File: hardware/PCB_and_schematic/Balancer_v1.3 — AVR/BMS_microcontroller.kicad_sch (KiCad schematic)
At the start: 73 parts, among them J12 V_MEAS, J13 LED, J14 ICP, J15 RS485, J16 RS485, Q21 BC817, U10 B0505S-1W, U11 ST485, U12 INA226, U4 AVR64DD28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

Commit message: add bms pcb balacer and smps separated
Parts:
- removed H2, H6, H8: MountingHole, My-Footprints:Mount-Hole-3mm, symbol Mechanical:MountingHole
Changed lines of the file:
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@@
 	)
 	(symbol
-		(lib_id "Mechanical:MountingHole")
-		(at 302.26 199.39 0)
-		(unit 1)
-		(exclude_from_sim yes)
-		(in_bom no)
-		(on_board yes)
-		(dnp no)
-		(fields_autoplaced yes)
-		(property "Reference" "H6"
-			(at 304.8 198.1199 0)
-			(effects
-				(font
-					(size 1.27 1.27)
-				)
-				(justify left)
-			)
-		)
-		(property "Value" "MountingHole"
-			(at 304.8 200.6599 0)
-			(effects
-				(font
-					(size 1.27 1.27)
-				)
-				(justify left)
-			)
-		)
-		(property "Footprint" "My-Footprints:Mount-Hole-3mm"
-			(at 302.26 199.39 0)
-			(effects
-				(font
-					(size 1.27 1.27)
-				)
-				(hide yes)
-			)
-		)
-		(property "Datasheet" "~"
-			(at 302.26 199.39 0)
-			(effects
-				(font
-					(size 1.27 1.27)
-				)
-				(hide yes)
-			)
-		)
-		(property "Description" "Mounting Hole without connection"
-			(at 302.26 199.39 0)
-			(effects
-				(font
-					(size 1.27 1.27)
-				)
-				(hide yes)
-			)
-		)
-		(instances
-			(project "Balancer"
-				(path "/555ba40f-9abb-4b99-82c6-07e888fda9fd/3b90ff07-e5cb-404b-939d-de320e975ba1"
-					(reference "H6")
-					(unit 1)
-				)
-			)
-		)
-	)
-	(symbol
 		(lib_id "power:GND")
 		(at 213.36 118.11 0)
@@
 	)
 	(symbol
-		(lib_id "Mechanical:MountingHole")
-		(at 280.67 214.63 0)
-		(unit 1)
-		(exclude_from_sim yes)
-		(in_bom no)
-		(on_board yes)
-		(dnp no)
-		(fields_autoplaced yes)
-		(property "Reference" "H2"
-			(at 283.21 213.3599 0)
-			(effects
-				(font
-					(size 1.27 1.27)
-				)
-				(justify left)
-			)
-		)
-		(property "Value" "MountingHole"
-			(at 283.21 215.8999 0)
-			(effects
-				(font
-					(size 1.27 1.27)
-				)
-				(justify left)
-			)
-		)
-		(property "Footprint" "My-Footprints:Mount-Hole-3mm"
-			(at 280.67 214.63 0)
-			(effects
-				(font
-					(size 1.27 1.27)
-				)
-				(hide yes)
-			)
-		)
-		(property "Datasheet" "~"
-			(at 280.67 214.63 0)
-			(effects
-				(font
-					(size 1.27 1.27)
-				)
-				(hide yes)
-			)
-		)
-		(property "Description" "Mounting Hole without connection"
-			(at 280.67 214.63 0)
-			(effects
-				(font
-					(size 1.27 1.27)
-				)
-				(hide yes)
-			)
-		)
-		(instances
-			(project "Balancer"
-				(path "/555ba40f-9abb-4b99-82c6-07e888fda9fd/3b90ff07-e5cb-404b-939d-de320e975ba1"
-					(reference "H2")
-					(unit 1)
-				)
-			)
-		)
-	)
-	(symbol
 		(lib_id "power:GND")
 		(at 273.05 106.68 0)
@@
 					(unit 1)
 				)
-			)
-		)
-	)
-	(symbol
-		(lib_id "Mechanical:MountingHole")
-		(at 302.26 209.55 0)
-		(unit 1)
-		(exclude_from_sim yes)
-		(in_bom no)
-		(on_board yes)
-		(dnp no)
-		(fields_autoplaced yes)
-		(property "Reference" "H8"
-			(at 304.8 208.2799 0)
-			(effects
-				(font
-					(size 1.27 1.27)
-				)
-				(justify left)
-			)
-		)
-		(property "Value" "MountingHole"
-			(at 304.8 210.8199 0)
-			(effects
-				(font
-					(size 1.27 1.27)
-				)
-				(justify left)
-			)
-		)
-		(property "Footprint" "My-Footprints:Mount-Hole-3mm"
-			(at 302.26 209.55 0)
-			(effects
-				(font
-					(size 1.27 1.27)
-				)
-				(hide yes)
-			)
-		)
-		(property "Datasheet" "~"
-			(at 302.26 209.55 0)
-			(effects
-				(font
-					(size 1.27 1.27)
-				)
-				(hide yes)
-			)
-		)
-		(property "Description" "Mounting Hole without connection"
-			(at 302.26 209.55 0)
-			(effects
-				(font
-					(size 1.27 1.27)
-				)
-				(hide yes)
-			)
-		)
-		(instances
-			(project "Balancer"
-				(path "/555ba40f-9abb-4b99-82c6-07e888fda9fd/3b90ff07-e5cb-404b-939d-de320e975ba1"
-					(reference "H8")
-					(unit 1)
-				)

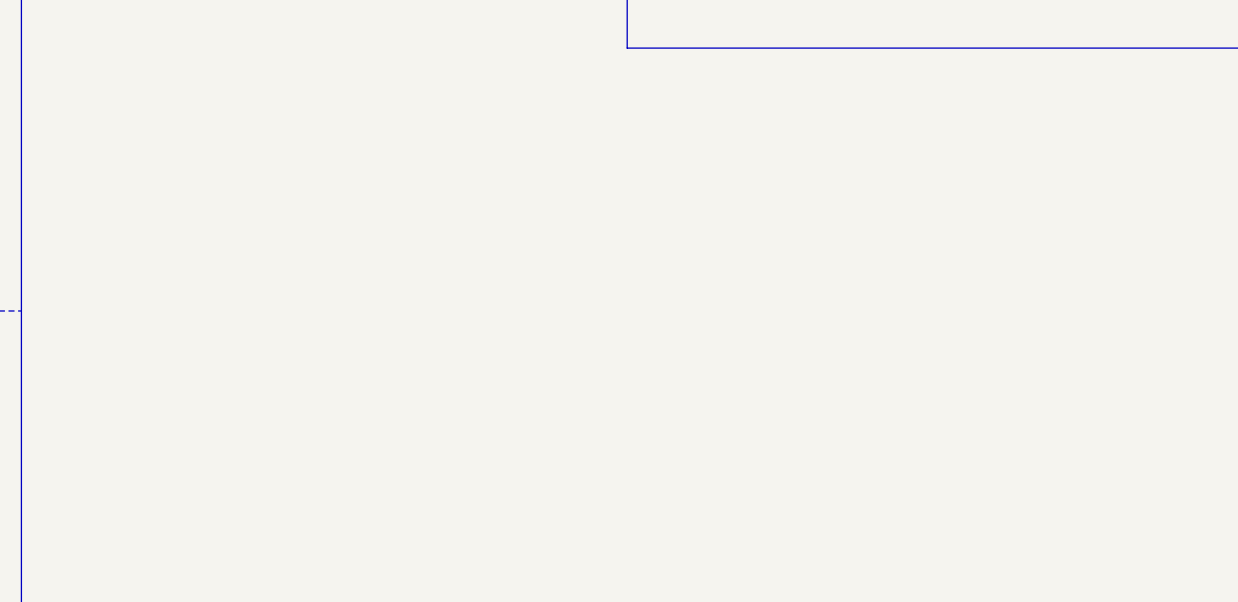
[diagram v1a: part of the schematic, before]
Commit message: routing power module
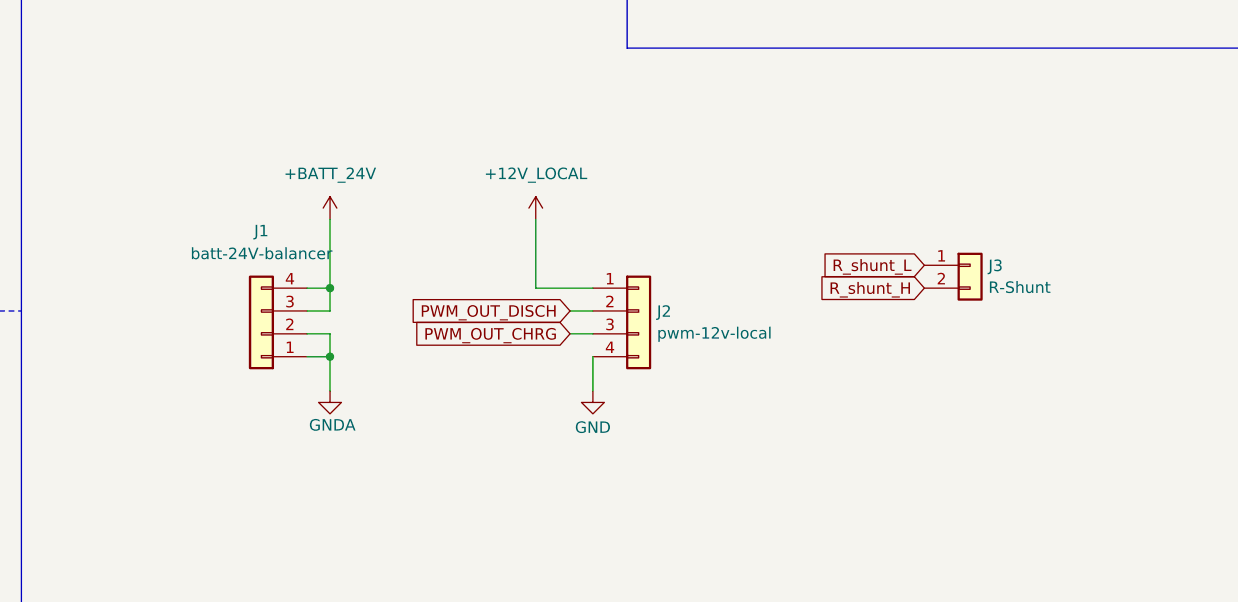
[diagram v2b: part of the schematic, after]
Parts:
- added J1: batt-24V-balancer, Connector_PinSocket_2.54mm:PinSocket_1x04_P2.54mm_Vertical, symbol Connector_Generic:Conn_01x04
- added J2: pwm-12v-local, Connector_PinSocket_2.54mm:PinSocket_1x04_P2.54mm_Vertical, symbol Connector_Generic:Conn_01x04
- added J3: R-Shunt, Connector_PinHeader_2.54mm:PinHeader_1x02_P2.54mm_Vertical, symbol Connector_Generic:Conn_01x02
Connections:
- net +12V_LOCAL: now also J2.1 (Pin_1)
- net +BATT_24V: now also J1.3 (Pin_3), J1.4 (Pin_4)
- net GND: now also J2.4 (Pin_4)
- net PWM_OUT_CHRG: now also J2.3 (Pin_3)
- net PWM_OUT_DISCH: now also J2.2 (Pin_2)
- net R_shunt_H: now also J3.2 (Pin_2)
- net R_shunt_L: now also J3.1 (Pin_1)
- new net GNDA: J1.1 (Pin_1), J1.2 (Pin_2)

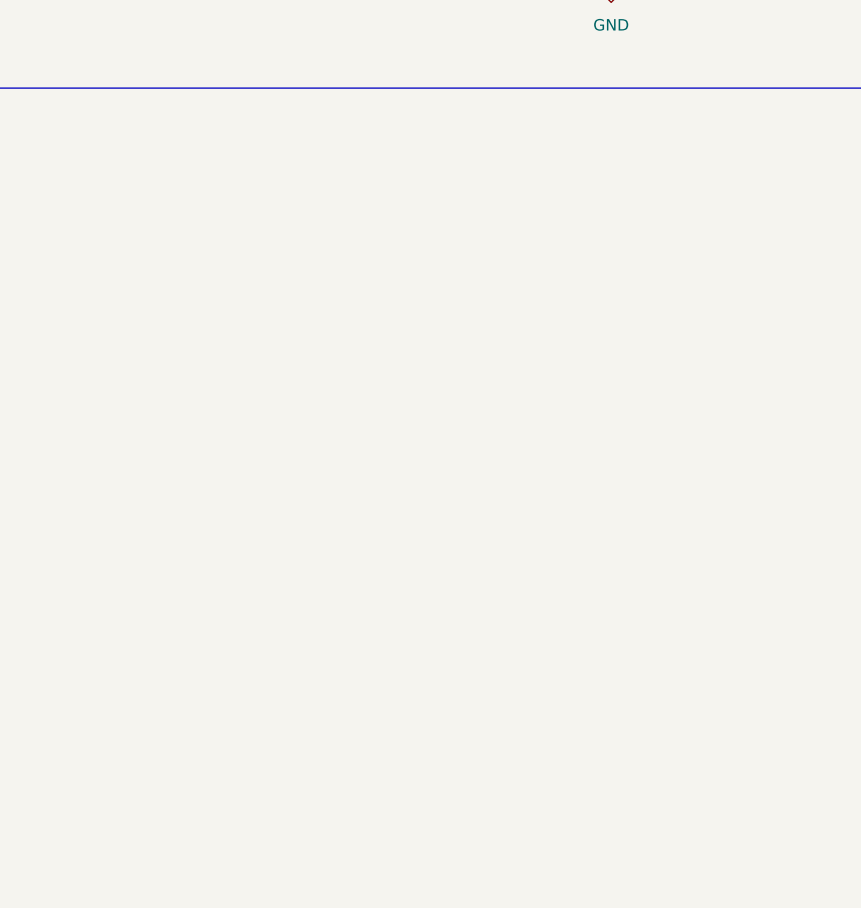
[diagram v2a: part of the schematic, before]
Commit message: done PCB power module and balancer
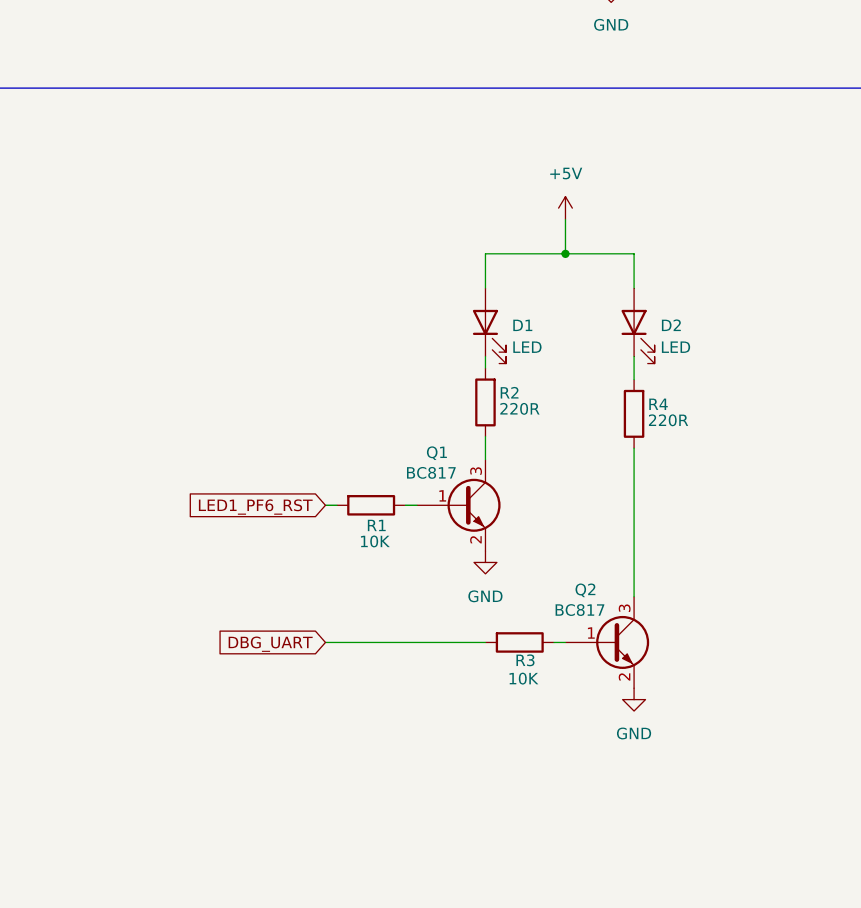
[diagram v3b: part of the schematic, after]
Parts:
- added D1, D2: LED, LED_THT:LED_D5.0mm, symbol Device:LED
- added Q1, Q2: BC817, Package_TO_SOT_SMD:SOT-23, symbol Transistor_BJT:BC817
- added R1, R3: 10K, Resistor_SMD:R_0805_2012Metric_Pad1.20x1.40mm_HandSolder, symbol Device:R
- added R2, R4: 220R, Resistor_SMD:R_0805_2012Metric_Pad1.20x1.40mm_HandSolder, symbol Device:R
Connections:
- net +5V: now also D1.2 (A), D2.2 (A)
- net DBG_UART: now also R3.2
- net GND: now also Q1.2 (E), Q2.2 (E)
- net LED1_PF6_RST: now also R1.2
- new net: Q2.1 (B), R3.1
- new net: Q1.1 (B), R1.1
- new net: Q2.3 (C), R4.1
- new net: D2.1 (K), R4.2
- new net: Q1.3 (C), R2.1
- new net: D1.1 (K), R2.2
